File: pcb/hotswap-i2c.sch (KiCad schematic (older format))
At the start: 6 parts, among them J1 Conn_01x04_Male, J2 Conn_01x02_Male, U1 TCA4311ADR

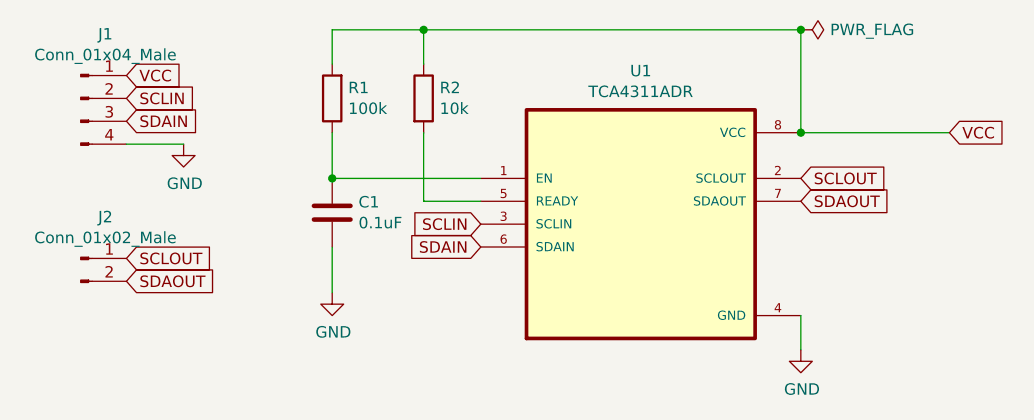
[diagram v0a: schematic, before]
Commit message: add decoupling cap
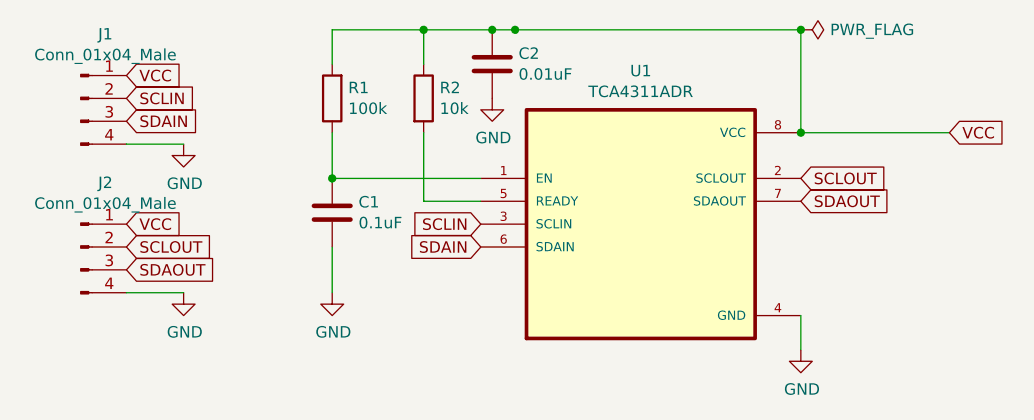
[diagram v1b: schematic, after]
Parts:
- removed J2: Conn_01x02_Male, Connector_PinHeader_2.54mm:PinHeader_1x02_P2.54mm_Vertical, symbol Connector:Conn_01x02_Male
- added C2: 0.01uF, Capacitor_SMD:C_0603_1608Metric_Pad1.05x0.95mm_HandSolder, symbol Device:C
- added J2: Conn_01x04_Male, Connector_PinHeader_2.54mm:PinHeader_1x04_P2.54mm_Vertical, symbol Connector:Conn_01x04_Male
- J1: footprint Connector_PinSocket_2.54mm:PinSocket_1x04_P2.54mm_Vertical -> Connector_PinHeader_2.54mm:PinHeader_1x04_P2.54mm_Vertical
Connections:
- net GND: now also C2.2, J2.4 (Pin_4)
- net SCLOUT: now also J2.2 (Pin_2)
- net SDAOUT: now also J2.3 (Pin_3)
- net VCC: now also C2.1, J2.1 (Pin_1)
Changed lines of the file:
@@
 Connection ~ 3900 1900
 Wire Wire Line
-	3900 1900 5550 1900
+	3900 1900 4200 1900
 Wire Wire Line
 	3900 2350 3900 2650
@@
 Text GLabel 5550 2650 2    50   Input ~ 0
 SDAOUT
-Text GLabel 2600 3000 2    50   Input ~ 0
+Text GLabel 2600 2950 2    50   Input ~ 0
 SDAOUT
-Text GLabel 2600 2900 2    50   Input ~ 0
+Text GLabel 2600 2850 2    50   Input ~ 0
 SCLOUT
 Text GLabel 2600 2300 2    50   Input ~ 0
@@
 Text GLabel 2600 2200 2    50   Input ~ 0
 SCLIN
-$Comp
-L Connector:Conn_01x02_Male J2
-U 1 1 5FD83AF1
-P 2400 2900
-F 0 "J2" H 2508 3081 50  0000 C CNN
-F 1 "Conn_01x02_Male" H 2508 2990 50  0000 C CNN
-F 2 "Connector_PinHeader_2.54mm:PinHeader_1x02_P2.54mm_Vertical" H 2400 2900 50  0001 C CNN
-F 3 "~" H 2400 2900 50  0001 C CNN
-	1    2400 2900
-	1    0    0    -1
-$EndComp
 Text GLabel 2600 2100 2    50   Input ~ 0
 VCC
@@
 Wire Wire Line
 	5550 3300 5550 3150
-$Comp
-L Connector:Conn_01x04_Male J1
-U 1 1 5FD6FF4C
-P 2400 2200
-F 0 "J1" H 2508 2481 50  0000 C CNN
-F 1 "Conn_01x04_Male" H 2508 2390 50  0000 C CNN
-F 2 "Connector_PinSocket_2.54mm:PinSocket_1x04_P2.54mm_Vertical" H 2400 2200 50  0001 C CNN
-F 3 "~" H 2400 2200 50  0001 C CNN
-	1    2400 2200
-	1    0    0    -1
-$EndComp
 Wire Wire Line
 	2600 2400 2850 2400
@@
 Text GLabel 6200 2350 2    50   Input ~ 0
 VCC
+$Comp
+L Connector:Conn_01x04_Male J1
+U 1 1 5FD6FF4C
+P 2400 2200
+F 0 "J1" H 2508 2481 50  0000 C CNN
+F 1 "Conn_01x04_Male" H 2508 2390 50  0000 C CNN
+F 2 "Connector_PinHeader_2.54mm:PinHeader_1x04_P2.54mm_Vertical" H 2400 2200 50  0001 C CNN
+F 3 "~" H 2400 2200 50  0001 C CNN
+	1    2400 2200
+	1    0    0    -1
+$EndComp
+Text GLabel 2600 2750 2    50   Input ~ 0
+VCC
+$Comp
+L power:GND #PWR01
+U 1 1 5FD6D635
+P 2850 3050
+F 0 "#PWR01" H 2850 2800 50  0001 C CNN
+F 1 "GND" H 2855 2877 50  0000 C CNN
+F 2 "" H 2850 3050 50  0001 C CNN
+F 3 "" H 2850 3050 50  0001 C CNN
+	1    2850 3050
+	1    0    0    -1
+$EndComp
+Wire Wire Line
+	2600 3050 2850 3050
+$Comp
+L Connector:Conn_01x04_Male J2
+U 1 1 5FD6D63C
+P 2400 2850
+F 0 "J2" H 2508 3131 50  0000 C CNN
+F 1 "Conn_01x04_Male" H 2508 3040 50  0000 C CNN
+F 2 "Connector_PinHeader_2.54mm:PinHeader_1x04_P2.54mm_Vertical" H 2400 2850 50  0001 C CNN
+F 3 "~" H 2400 2850 50  0001 C CNN
+	1    2400 2850
+	1    0    0    -1
+$EndComp
+$Comp
+L Device:C C2
+U 1 1 5FD6BC2E
+P 4200 2050
+F 0 "C2" H 4315 2096 50  0000 L CNN
+F 1 "0.01uF" H 4315 2005 50  0000 L CNN
+F 2 "Capacitor_SMD:C_0603_1608Metric_Pad1.05x0.95mm_HandSolder" H 4238 1900 50  0001 C CNN
+F 3 "~" H 4200 2050 50  0001 C CNN
+	1    4200 2050
+	1    0    0    -1
+$EndComp
+Connection ~ 4300 1900
+Wire Wire Line
+	4300 1900 5550 1900
+$Comp
+L power:GND #PWR0104
+U 1 1 5FD6CB04
+P 4200 2200
+F 0 "#PWR0104" H 4200 1950 50  0001 C CNN
+F 1 "GND" H 4205 2027 50  0000 C CNN
+F 2 "" H 4200 2200 50  0001 C CNN
+F 3 "" H 4200 2200 50  0001 C CNN
+	1    4200 2200
+	1    0    0    -1
+$EndComp
+Connection ~ 4200 1900
+Wire Wire Line
+	4200 1900 4300 1900
 $EndSCHEMATC
